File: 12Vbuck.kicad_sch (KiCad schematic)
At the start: 33 parts, among them Q1 NMOS, Q2 NMOS, U1 LM5146RGYR

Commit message: lagt til alle komponenter og størrelser
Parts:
- C302: value 47nF -> 12.5n
- C303: footprint (none) -> Capacitor_SMD:C_0201_0603Metric; Field6 (none) -> EMK107BB7225KA-T
- C304: footprint (none) -> Capacitor_SMD:C_0201_0603Metric; Field6 (none) -> TMK107B7104KAHT
- C305: footprint (none) -> Capacitor_SMD:C_0201_0603Metric; Field6 (none) -> GCM1885C1H100FA16D
- C306: value 4.7n -> 5.6n; footprint (none) -> Capacitor_SMD:C_0201_0603Metric; Field6 (none) -> CC0603JRNPO9BN562
- C307: value 100p -> 82p; footprint (none) -> Capacitor_SMD:C_0201_0603Metric; Field6 (none) -> GCM1885C2A820FA16D
- C308: value 1n -> 1.3n; footprint (none) -> Capacitor_SMD:C_0201_0603Metric; Field6 (none) -> GCM1885C1H132GA16D
- C309: footprint (none) -> Capacitor_SMD:C_1210_3225Metric; del (none) -> GRM32ER72A225KA35L
- C310: Field6 (none) -> GRM32ER72A225KA35L
- C311, C312, C313: footprint (none) -> Capacitor_SMD:C_1210_3225Metric; Field6 (none) -> GRM32ER72A225KA35L
- C314: footprint (none) -> Capacitor_SMD:C_0805_2012Metric; Field6 (none) -> GMK212B7105MG-T
- C315, C316: footprint (none) -> Capacitor_SMD:C_1206_3216Metric; Field6 (none) -> MSASG31LAB7106MTNB25
- L301: footprint Package_SO:SSOP-16_3.9x4.9mm_P0.635mm -> CAPAE830X1000N; symbol Device:L -> Halfdan:APA0809470M050R; Height (none) -> 10; Manufacturer_Name (none) -> Kyocera AVX; Manufacturer_Part_Number (none) -> APA0809470M050R; Mouser Part Number (none) -> 581-APA0809470M050R; Mouser Price/Stock (none) -> https://www.mouser.co.uk/ProductDetail/KYOCERA-AVX/APA08094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
- R301: footprint (none) -> Resistor_SMD:R_0201_0603Metric; Field6 (none) -> RC0603FR-079K31L
- R302: footprint (none) -> Resistor_SMD:R_0201_0603Metric; Field6 (none) -> RM06F1003CT
- R303, R304: footprint (none) -> Resistor_SMD:R_0201_0603Metric; Field6 (none) -> RK73H1JTTD2R20F
- R305: footprint (none) -> Resistor_SMD:R_0201_0603Metric; Field6 (none) -> RT0603BRD0724K9L
- R306: footprint (none) -> Resistor_SMD:R_0201_0603Metric; Field6 (none) -> RT0603BRD07619RL
- R307: value 8.06k -> 9.76k; footprint (none) -> Resistor_SMD:R_0201_0603Metric; Field6 (none) -> CRCW06039K76FKEA
- R308: footprint (none) -> Resistor_SMD:R_0201_0603Metric; Field6 (none) -> RG1608P-152-B-T5
- R309: footprint (none) -> Resistor_SMD:R_0201_0603Metric; Field6 (none) -> RT0603DRD0721KL
- R310: value 100k -> 100; footprint (none) -> Resistor_SMD:R_0201_0603Metric; Field6 (none) -> CRCW0603100RFKEA
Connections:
- net 12V_Vout: now also C317.1 (+), C318.1 (+); no longer C317.2 (-), C318.2 (-)
- net PGND: now also C317.2 (-), C318.2 (-); no longer C317.1 (+), C318.1 (+)
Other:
- moved on the sheet: C309, C310, C311, C312, C313, C314, C315, C316, C317, C318

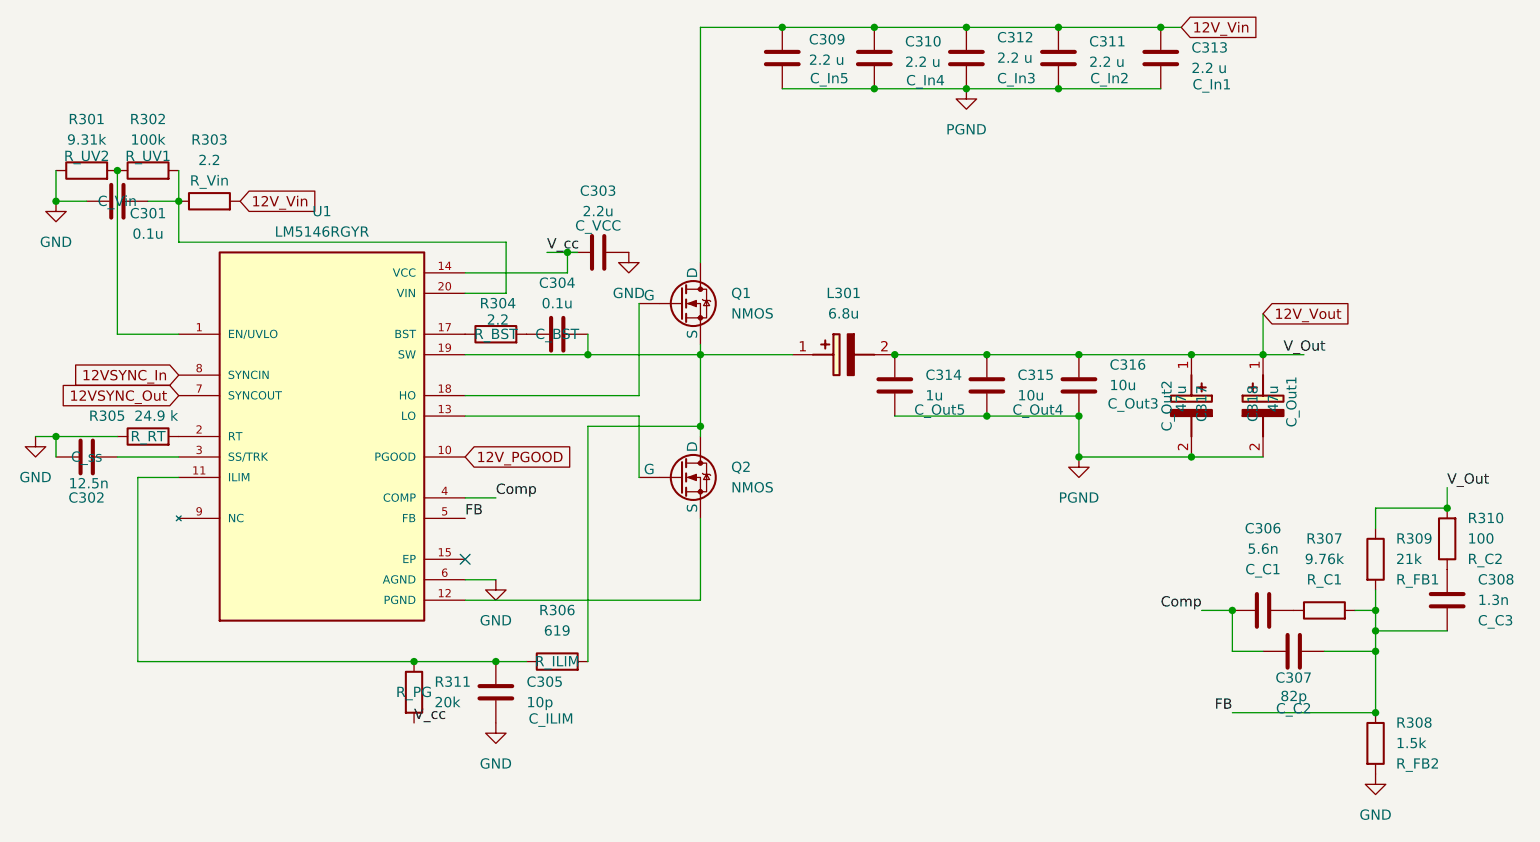
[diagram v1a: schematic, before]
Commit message: alle komponenter har fått rett navn
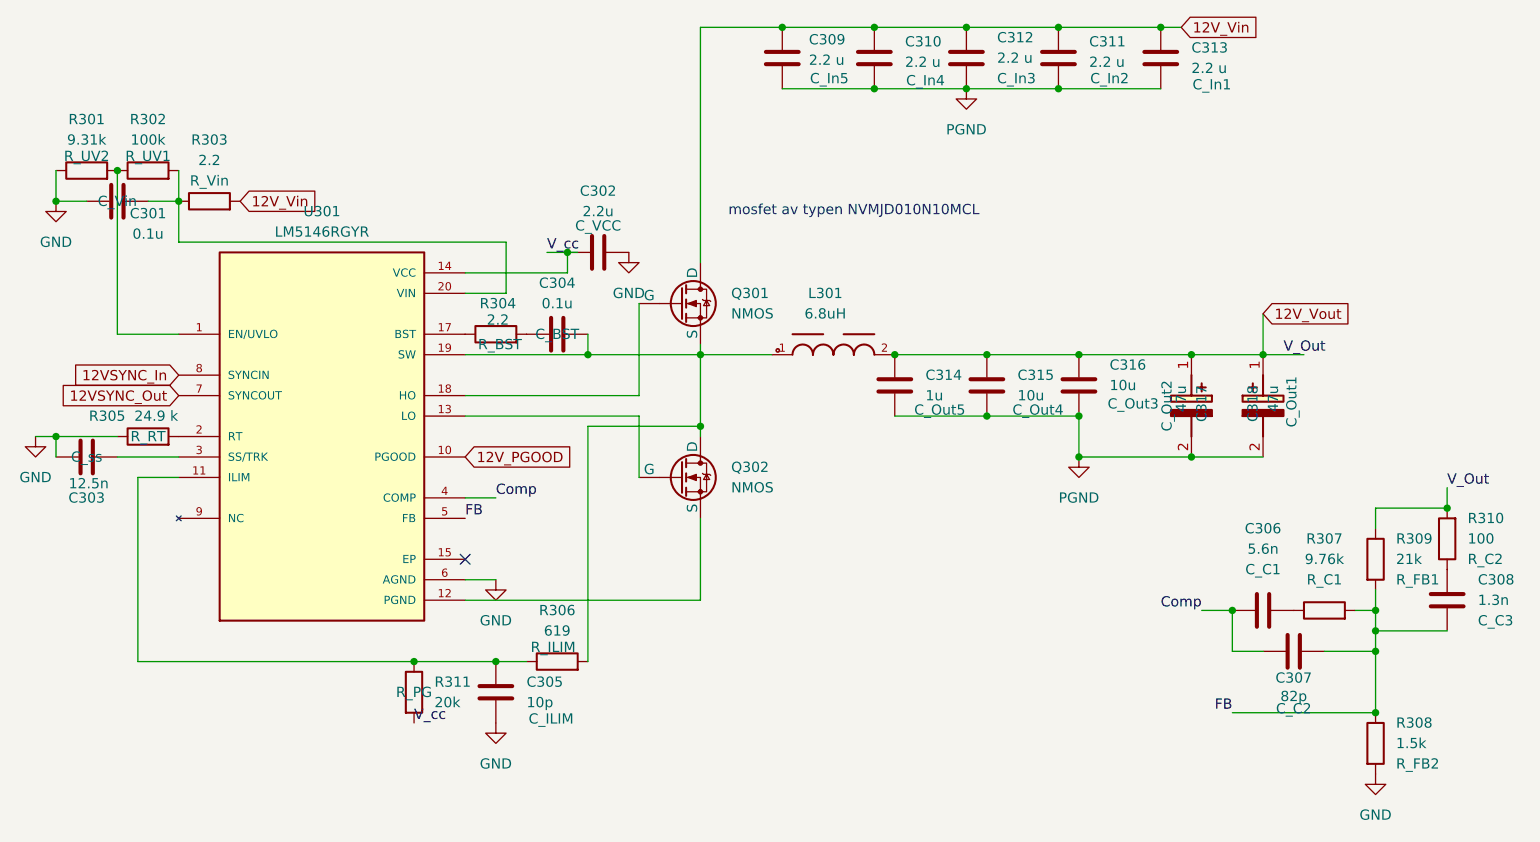
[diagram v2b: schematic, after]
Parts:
- removed L301: 6.8u, CAPAE830X1000N, symbol Halfdan:APA0809470M050R
- added L301: 6.8uH, WE-XHMA_1510:WE-XHMA_1510, symbol Halfdan:WE-XHMA_1510
- C309: del GRM32ER72A225KA35L -> HMK325B7225KN-T
- C310, C311, C312, C313: Field6 GRM32ER72A225KA35L -> HMK325B7225KN-T
- renumbered C303 to C302, C302 to C303, Q1 to Q301, Q2 to Q302, U1 to U301
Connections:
- net 12V_Vout: now also L301.2
- net at C304.2, Q301.3 (S), Q302.1 (D)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: now also L301.1
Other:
- note added: "mosfet av typen NVMJD010N10MCL"
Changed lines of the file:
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@@
 	(generator_version "10.0")
 	(paper "A4")
+	(text "mosfet av typen NVMJD010N10MCL\n\n"
+		(exclude_from_sim no)
+		(at 186.69 74.676 0)
+		(effects
+			(font
+				(size 1.27 1.27)
+			)
+		)
+	)
 	(junction
 		(at 167.64 100.33)
@@
 	)
 	(junction
-		(at 191.77 91.44)
-		(diameter 0)
-		(color 0 0 0 0)
-	)
-	(junction
 		(at 212.09 50.8)
 		(diameter 0)
@@
 	)
 	(junction
+		(at 191.77 91.44)
+		(diameter 0)
+		(color 0 0 0 0)
+	)
+	(junction
 		(at 200.66 50.8)
 		(diameter 0)
@@
 	(wire
 		(pts
-			(xy 167.64 91.44) (xy 179.07 91.44)
-		)
-		(stroke
-			(width 0)
-			(type default)
-		)
-	)
-	(wire
-		(pts
 			(xy 167.64 50.8) (xy 167.64 80.01)
 		)
@@
 	(wire
 		(pts
+			(xy 167.64 91.44) (xy 176.53 91.44)
+		)
+		(stroke
+			(width 0)
+			(type default)
+		)
+	)
+	(wire
+		(pts
 			(xy 248.92 123.19) (xy 251.46 123.19)
 		)
@@
 		(in_pos_files yes)
 		(dnp no)
-		(property "Reference" "C303"
+		(property "Reference" "C302"
 			(at 154.94 71.12 90)
 			(show_name no)
@@
 			(project "ProteusPowerManagment"
 				(path "/c24111dd-5300-4143-a3c3-2d963194a3cb/c1246cae-1020-4e2b-a9f1-a2035453bc0c"
-					(reference "C303")
+					(reference "C302")
 					(unit 1)
 				)
@@
 		)
 		(property "Field5" "R_BST"
-			(at 142.24 88.9 90)
+			(at 142.748 90.17 90)
 			(show_name no)
 			(do_not_autoplace no)
@@
 			)
 		)
-		(property "Field6" "GRM32ER72A225KA35L"
+		(property "Field6" "HMK325B7225KN-T"
 			(at 189.23 54.61 0)
 			(hide yes)
@@
 		(in_pos_files yes)
 		(dnp no)
-		(property "Reference" "C302"
+		(property "Reference" "C303"
 			(at 91.44 109.22 90)
 			(show_name no)
@@
 			(project "ProteusPowerManagment"
 				(path "/c24111dd-5300-4143-a3c3-2d963194a3cb/c1246cae-1020-4e2b-a9f1-a2035453bc0c"
-					(reference "C302")
+					(reference "C303")
 					(unit 1)
 				)
@@
 			)
 		)
-		(property "Field6" "GRM32ER72A225KA35L"
+		(property "Field6" "HMK325B7225KN-T"
 			(at 224.79 54.61 0)
 			(hide yes)
@@
 			)
 		)
-		(property "Field6" "GRM32ER72A225KA35L"
+		(property "Field6" "HMK325B7225KN-T"
 			(at 212.09 54.61 0)
 			(hide yes)
@@
 	)
 	(symbol
-		(lib_id "Halfdan:APA0809470M050R")
-		(at 179.07 91.44 0)
-		(unit 1)
-		(body_style 1)
-		(exclude_from_sim no)
-		(in_bom yes)
-		(on_board yes)
-		(in_pos_files yes)
-		(dnp no)
-		(fields_autoplaced yes)
-		(property "Reference" "L301"
-			(at 185.42 83.82 0)
-			(show_name no)
-			(do_not_autoplace no)
-			(effects
-				(font
-					(size 1.27 1.27)
-				)
-			)
-		)
-		(property "Value" "6.8u"
-			(at 185.42 86.36 0)
-			(show_name no)
-			(do_not_autoplace no)
-			(effects
-				(font
-					(size 1.27 1.27)
-				)
-			)
-		)
-		(property "Footprint" "CAPAE830X1000N"
-			(at 187.96 187.63 0)
-			(hide yes)
-			(show_name no)
-			(do_not_autoplace no)
-			(effects
-				(font
-					(size 1.27 1.27)
-				)
-				(justify left top)
-			)
-		)
-		(property "Datasheet" "https://datasheets.kyocera-avx.com/kyocera-avx-apa-series.pdf"
-			(at 187.96 287.63 0)
-			(hide yes)
-			(show_name no)
-			(do_not_autoplace no)
-			(effects
-				(font
-					(size 1.27 1.27)
-				)
-				(justify left top)
-			)
-		)
-		(property "Description" "Aluminum Organic Polymer Capacitors 47UF       50V"
-			(at 179.07 91.44 0)
-			(hide yes)
-			(show_name no)
-			(do_not_autoplace no)
-			(effects
-				(font
-					(size 1.27 1.27)
-				)
-			)
-		)
-		(property "Height" "10"
-			(at 187.96 487.63 0)
-			(hide yes)
-			(show_name no)
-			(do_not_autoplace no)
-			(effects
-				(font
-					(size 1.27 1.27)
-				)
-				(justify left top)
-			)
-		)
-		(property "Mouser Part Number" "581-APA0809470M050R"
-			(at 187.96 587.63 0)
-			(hide yes)
-			(show_name no)
-			(do_not_autoplace no)
-			(effects
-				(font
-					(size 1.27 1.27)
-				)
-				(justify left top)
-			)
-		)
-		(property "Mouser Price/Stock" "https://www.mouser.co.uk/ProductDetail/KYOCERA-AVX/APA0809470M050R?qs=Wj%2FVkw3K%252BMAkqelysx9Hrg%3D%3D"
-			(at 187.96 687.63 0)
-			(hide yes)
-			(show_name no)
-			(do_not_autoplace no)
-			(effects
-				(font
-					(size 1.27 1.27)
-				)
-				(justify left top)
-			)
-		)
-		(property "Manufacturer_Name" "Kyocera AVX"
-			(at 187.96 787.63 0)
-			(hide yes)
-			(show_name no)
-			(do_not_autoplace no)
-			(effects
-				(font
-					(size 1.27 1.27)
-				)
-				(justify left top)
-			)
-		)
-		(property "Manufacturer_Part_Number" "APA0809470M050R"
-			(at 187.96 887.63 0)
-			(hide yes)
-			(show_name no)
-			(do_not_autoplace no)
-			(effects
-				(font
-					(size 1.27 1.27)
-				)
-				(justify left top)
-			)
-		)
-		(pin "1"
-		)
-		(pin "2"
-		)
-		(instances
-			(project "ProteusPowerManagment"
-				(path "/c24111dd-5300-4143-a3c3-2d963194a3cb/c1246cae-1020-4e2b-a9f1-a2035453bc0c"
-					(reference "L301")
-					(unit 1)
-				)
-			)
-		)
-	)
-	(symbol
 		(lib_id "power:GND")
 		(at 87.63 72.39 0)
@@
 		(dnp no)
 		(fields_autoplaced yes)
-		(property "Reference" "Q1"
+		(property "Reference" "Q301"
 			(at 171.45 83.8199 0)
 			(show_name no)
@@
 			(project "ProteusPowerManagment"
 				(path "/c24111dd-5300-4143-a3c3-2d963194a3cb/c1246cae-1020-4e2b-a9f1-a2035453bc0c"
-					(reference "Q1")
+					(reference "Q301")
 					(unit 1)
 				)
@@
 		(in_pos_files yes)
 		(dnp no)
-		(fields_autoplaced yes)
 		(property "Reference" "R306"
 			(at 149.86 123.19 90)
@@
 		)
 		(property "Field5" "R_ILIM"
-			(at 149.86 129.54 90)
+			(at 149.352 127.762 90)
 			(show_name no)
 			(do_not_autoplace no)
@@
 			)
 		)
-		(property "Field6" "GRM32ER72A225KA35L"
+		(property "Field6" "HMK325B7225KN-T"
 			(at 200.66 54.61 0)
 			(hide yes)
@@
 			)
 		)
-		(property "del" "GRM32ER72A225KA35L"
+		(property "del" "HMK325B7225KN-T"
 			(at 177.8 54.61 0)
 			(hide yes)
@@
 		(dnp no)
 		(fields_autoplaced yes)
-		(property "Reference" "Q2"
+		(property "Reference" "Q302"
 			(at 171.45 105.4099 0)
 			(show_name no)
@@
 			(project "ProteusPowerManagment"
 				(path "/c24111dd-5300-4143-a3c3-2d963194a3cb/c1246cae-1020-4e2b-a9f1-a2035453bc0c"
-					(reference "Q2")
+					(reference "Q302")
 					(unit 1)
 				)
@@
 		(dnp no)
 		(fields_autoplaced yes)
-		(property "Reference" "U1"
+		(property "Reference" "U301"
 			(at 120.65 73.66 0)
 			(show_name no)
@@
 			(project "ProteusPowerManagment"
 				(path "/c24111dd-5300-4143-a3c3-2d963194a3cb/c1246cae-1020-4e2b-a9f1-a2035453bc0c"
-					(reference "U1")
+					(reference "U301")
 					(unit 1)
 				)
@@
 					(unit 1)
 				)
+			)
+		)
+	)
+	(symbol
+		(lib_id "Halfdan:WE-XHMA_1510")
+		(at 184.15 91.44 0)
+		(unit 1)
+		(body_style 1)
+		(exclude_from_sim no)
+		(in_bom yes)
+		(on_board yes)
+		(in_pos_files yes)
+		(dnp no)
+		(fields_autoplaced yes)
+		(property "Reference" "L301"
+			(at 183.1479 83.82 0)
+			(show_name no)
+			(do_not_autoplace no)
+			(effects
+				(font
+					(size 1.27 1.27)
+				)
+			)
+		)
+		(property "Value" "6.8uH"
+			(at 183.1479 86.36 0)
+			(show_name no)
+			(do_not_autoplace no)
+			(effects
+				(font
+					(size 1.27 1.27)
+				)
+			)
+		)
+		(property "Footprint" "WE-XHMA_1510:WE-XHMA_1510"
+			(at 184.15 91.44 0)
+			(hide yes)
+			(show_name no)
+			(do_not_autoplace no)
+			(effects
+				(font
+					(size 1.27 1.27)
+				)
+				(justify bottom)
+			)
+		)
+		(property "Datasheet" ""
+			(at 184.15 91.44 0)
+			(hide yes)
+			(show_name no)
+			(do_not_autoplace no)
+			(effects
+				(font
+					(size 1.27 1.27)
+				)
+			)
+		)
+		(property "Description" ""
+			(at 184.15 91.44 0)
+			(hide yes)
+			(show_name no)
+			(do_not_autoplace no)
+			(effects
+				(font
+					(size 1.27 1.27)
+				)
+			)
+		)
+		(pin "1"
+		)
+		(pin "2"
+		)
+		(instances
+			(project "ProteusPowerManagment"
+				(path "/c24111dd-5300-4143-a3c3-2d963194a3cb/c1246cae-1020-4e2b-a9f1-a2035453bc0c"
+					(reference "L301")
+					(unit 1)
+				)

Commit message: måtte endre på footprints i 5v da de ikke var lik BOM
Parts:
- C301, C303: footprint (none) -> Capacitor_SMD:C_0201_0603Metric
- R311: footprint (none) -> Resistor_SMD:R_0201_0603Metric
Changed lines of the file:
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@@
 			)
 		)
-		(property "Footprint" ""
+		(property "Footprint" "Resistor_SMD:R_0201_0603Metric"
 			(at 130.302 133.35 90)
 			(hide yes)
@@
 			)
 		)
-		(property "Footprint" ""
+		(property "Footprint" "Capacitor_SMD:C_0201_0603Metric"
 			(at 95.25 103.1748 0)
 			(hide yes)
@@
 			)
 		)
-		(property "Footprint" ""
+		(property "Footprint" "Capacitor_SMD:C_0201_0603Metric"
 			(at 99.06 71.4248 0)
 			(hide yes)
